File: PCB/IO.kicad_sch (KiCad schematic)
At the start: 18 parts, among them J6 USB_1, J7 USB_2, U11 FUSB_1, U13 FUSB_2, U5 TS3USB_2, U7 TS3USB_1

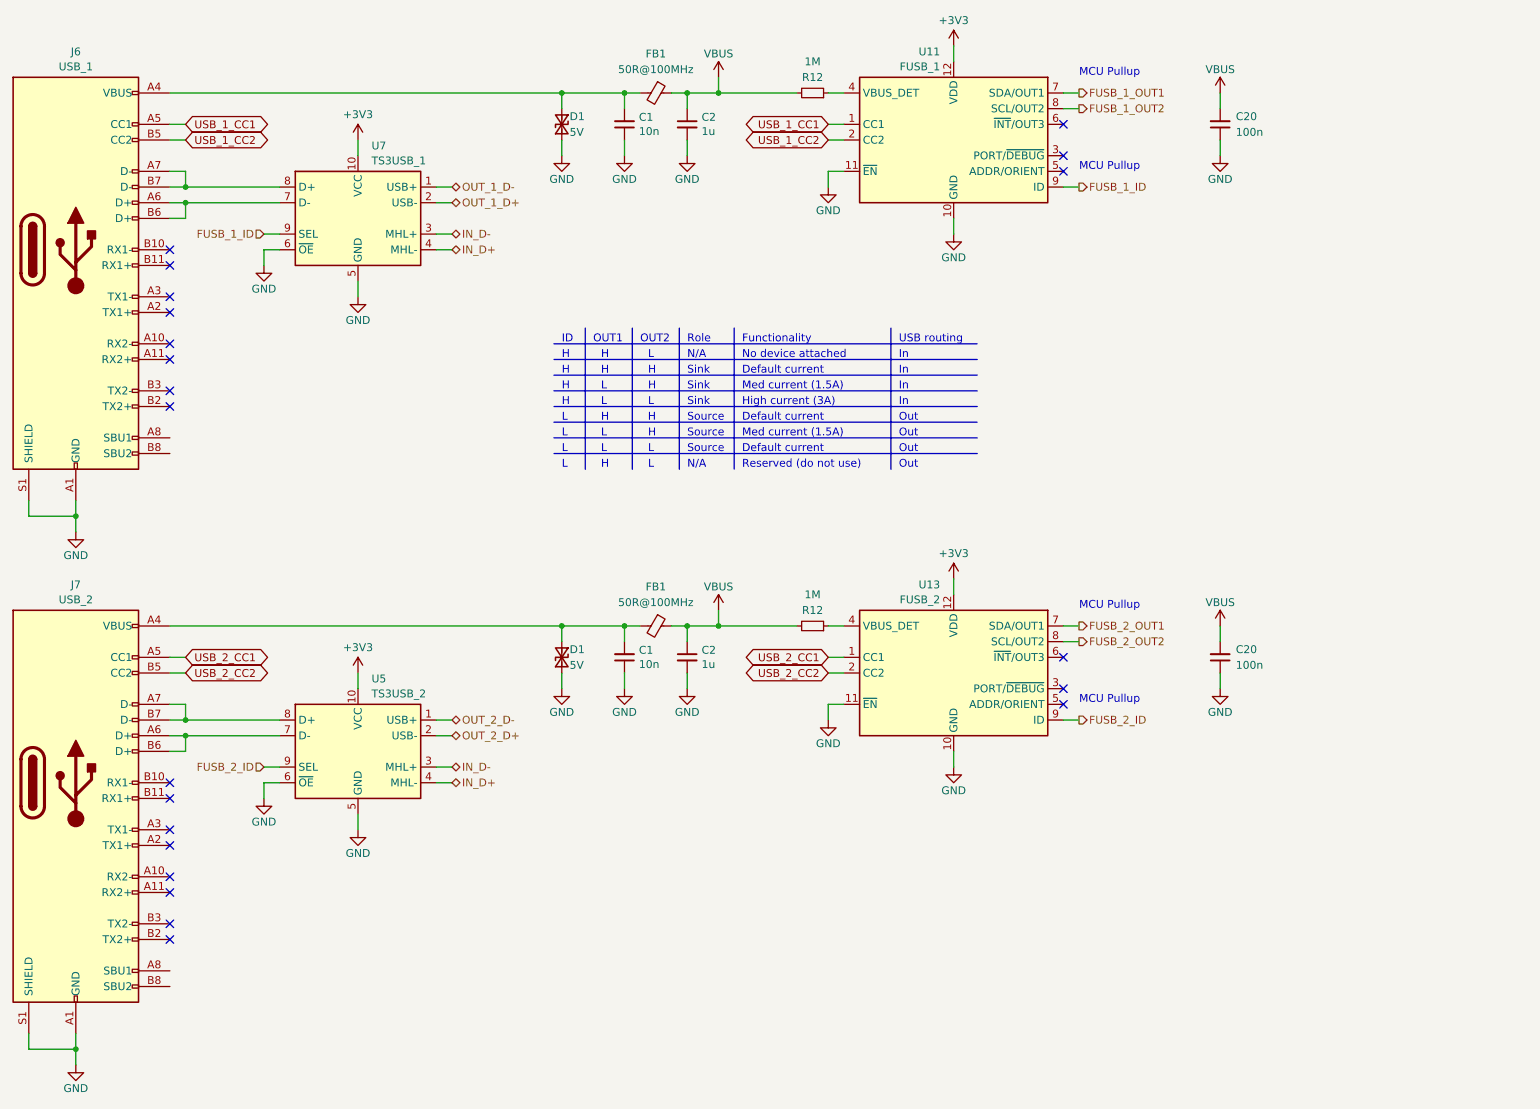
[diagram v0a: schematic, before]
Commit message: 23/08/2023 update
Changed MCU to nRF52840. Added nPM1300 PMIC for power management. Replaced SSD1351 display with Nice!View. Added Kailh Choc V1/V2 and Gateron KS-27/KS-33 support.
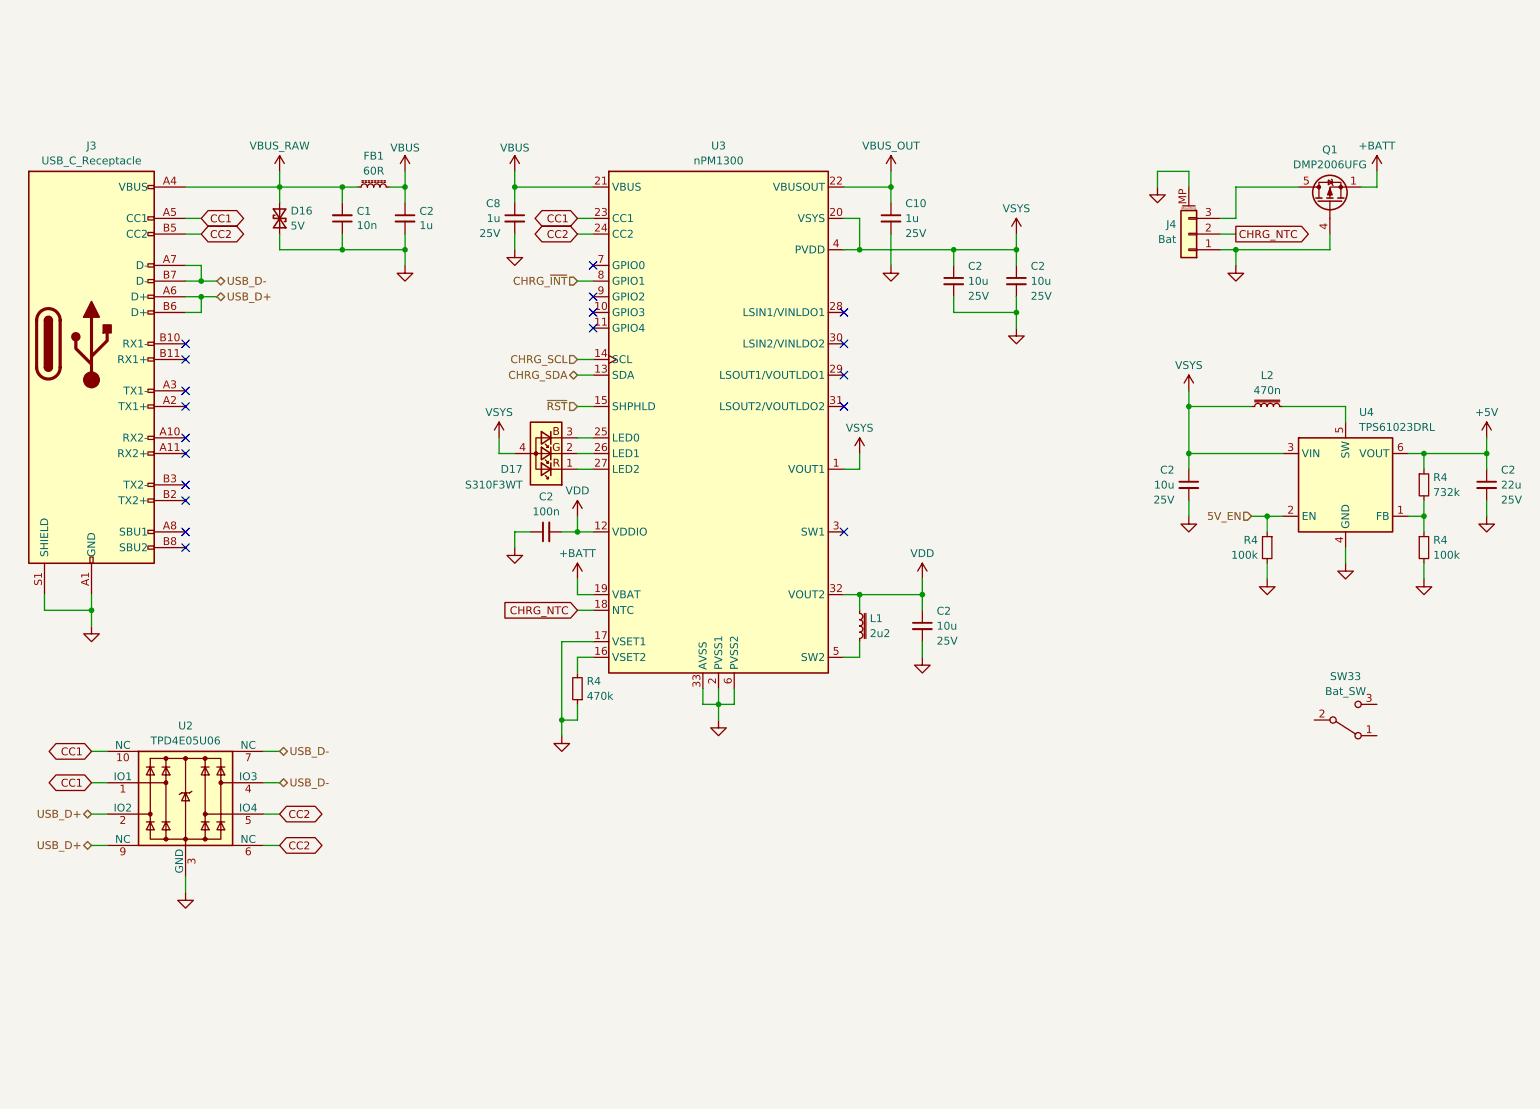
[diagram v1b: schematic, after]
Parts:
- removed C1 (x2): 10n, Capacitor_SMD:C_0402_1005Metric, symbol Device:C_Small
- removed C2 (x2): 1u, Capacitor_SMD:C_0603_1608Metric, symbol Device:C_Small
- removed C20 (x2): 100n, Capacitor_SMD:C_0402_1005Metric, symbol Device:C_Small
- removed D1 (x2): 5V, Diode_SMD:D_SOD-523, symbol Galia:D_TVS_Small
- removed FB1 (x2): 50R@100MHz, Inductor_SMD:L_1206_3216Metric, symbol Device:FerriteBead_Small
- removed J6: USB_1, symbol Connector:USB_C_Receptacle
- removed J7: USB_2, symbol Connector:USB_C_Receptacle
- removed R12 (x2): 1M, Resistor_SMD:R_0402_1005Metric, symbol Device:R_Small
- removed U11: FUSB_1, Package_DFN_QFN:Texas_X2QFN-12_1.6x1.6mm_P0.4mm, symbol Cantaloupe:FUSB303B
- removed U13: FUSB_2, Package_DFN_QFN:Texas_X2QFN-12_1.6x1.6mm_P0.4mm, symbol Cantaloupe:FUSB303B
- removed U5: TS3USB_2, symbol Cantaloupe:TS3USB3000
- removed U7: TS3USB_1, symbol Cantaloupe:TS3USB3000
- added C1: 10n, Ariamelon-Device:C_0402_1005Metric, symbol Device:C_Small
- added C10, C8: 1u, Ariamelon-Device:C_0402_1005Metric, symbol Device:C_Small
- added C2: 100n, Ariamelon-Device:C_0402_1005Metric, symbol Device:C_Small
- added C2 (x4): 10u, Ariamelon-Device:C_0603_1608Metric, symbol Device:C_Small
- added C2: 1u, Ariamelon-Device:C_0603_1608Metric, symbol Device:C_Small
- added C2: 22u, Ariamelon-Device:C_0805_2012Metric, symbol Device:C_Small
- added D16: 5V, Diode_SMD:D_SOD-523, symbol Ariamelon-Device:D_TVS_Small
- added D17: S310F3WT, Ariamelon-Device:LED_Lite-On_LTST-S310_3x1.5mm_Horizontal, symbol Ariamelon-Device:LED_ABGR_Small
- added FB1: 60R, Ariamelon-Device:L_0805_2012Metric, symbol Device:L_Ferrite_Small
- added J3: USB_C_Receptacle, Ariamelon-Connector:Hirose_CX70M-24P1, symbol Connector:USB_C_Receptacle
- added J4: Bat, Ariamelon-Connector:JST_SH_SM03B-SRSS-TB_1x03-1MP_P1.00mm_Horizontal, symbol Connector_Generic_MountingPin:Conn_01x03_MountingPin
- added L1: 2u2, Ariamelon-Device:L_Murata_DFE201610P, symbol Device:L_Iron_Small
- added L2: 470n, Ariamelon-Device:L_Murata_DFE201610P, symbol Device:L_Iron_Small
- added Q1: DMP2006UFG, Ariamelon-Package:Diodes_PowerDI3333-8, symbol Transistor_FET:DMP3013SFV
- added R4: 732k, Ariamelon-Device:R_0402_1005Metric, symbol Device:R_Small
- added R4: 470k, Ariamelon-Device:R_0402_1005Metric, symbol Device:R_Small
- added R4 (x2): 100k, Ariamelon-Device:R_0402_1005Metric, symbol Device:R_Small
- added SW33: Bat_SW, Button_Switch_SMD:SW_SPDT_PCM12, symbol Switch:SW_SPDT
- added U2: TPD4E05U06, Ariamelon-Package:USON-10_2.5x1.0mm_P0.5mm, symbol Ariamelon-IC:TPD4E05U06
- added U3: nPM1300, Ariamelon-Package:QFN-32-1EP_5x5mm_P0.5mm_EP3.5x3.5mm, symbol Ariamelon-IC:nPM1300
- added U4: TPS61023DRL, Ariamelon-Package:SOT-563, symbol Ariamelon-IC:TPS61023DRL
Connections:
- net GND: now also C1.1, C10.2, C2.1, C2.2, C2.2, C2.2, C2.2, C2.2, C2.2, C8.2, D16.1 (K), J3.A1 (GND), J3.A12 (GND), J3.B1 (GND), J3.B12 (GND), J3.S1 (SHIELD), J4.1 (Pin_1), J4.MP (MountPin), Q1.4 (G), R4.1, R4.2, R4.2, U2.3 (GND), U2.8 (GND), U3.17 (VSET1), U3.2 (PVSS1), U3.33 (AVSS), U3.6 (PVSS2), U4.4 (GND)
- net VBUS: now also C2.1, C8.1, FB1.1, U3.21 (VBUS)
- new net: D17.1 (RK), U3.27 (LED2)
- new net: D17.2 (GK), U3.26 (LED1)
- new net: D17.3 (BK), U3.25 (LED0)
- new net: R4.1, R4.2, U4.1 (FB)
- new net: L2.2, U4.5 (SW)
- new net: J4.3 (Pin_3), Q1.5 (D)
- new net: R4.2, U3.16 (VSET2)
- new net: L1.2, U3.5 (SW2)
- new net +5V: C2.1, R4.1, U4.6 (VOUT)
- new net +BATT: Q1.1 (S), Q1.2 (S), Q1.3 (S), U3.19 (VBAT)
- new net 5V_EN: R4.1, U4.2 (EN)
- new net CC1: J3.A5 (CC1), U2.1 (IO1), U2.10 (NC), U3.23 (CC1)
- new net CC2: J3.B5 (CC2), U2.5 (IO4), U2.6 (NC), U3.24 (CC2)
- new net CHRG_NTC: J4.2 (Pin_2), U3.18 (NTC)
- new net CHRG_SCL: U3.14 (SCL)
- new net CHRG_SDA: U3.13 (SDA)
- new net CHRG_~{INT}: U3.8 (GPIO1)
- new net USB_D+: J3.A6 (D+), J3.B6 (D+), U2.2 (IO2), U2.9 (NC)
- new net USB_D-: J3.A7 (D-), J3.B7 (D-), U2.4 (IO3), U2.7 (NC)
- new net VBUS_OUT: C10.1, U3.22 (VBUSOUT)
- new net VBUS_RAW: C1.2, D16.2 (A), FB1.2, J3.A4 (VBUS), J3.A9 (VBUS), J3.B4 (VBUS), J3.B9 (VBUS)
- new net VDD: C2.1, C2.2, L1.1, U3.12 (VDDIO), U3.32 (VOUT2)
- new net VSYS: C2.1, C2.1, C2.1, D17.4 (A), L2.1, U3.1 (VOUT1), U3.20 (VSYS), U3.4 (PVDD), U4.3 (VIN)
- new net ~{RST}: U3.15 (SHPHLD)
- no-connect marks 22 -> 19
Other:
- note removed: "Default current"
- note removed: "Functionality"
- note removed: "H"
- note removed: "High current (3A)"
- note removed: "ID"
- note removed: "In"
- note removed: "L"
- note removed: "MCU Pullup"
- note removed: "Med current (1.5A)"
- note removed: "N/A"
- note removed: "No device attached"
- note removed: "OUT1"
- note removed: "OUT2"
- note removed: "Out"
- note removed: "Reserved (do not use)"
- note removed: "Role"
- note removed: "Sink"
- note removed: "Source"
- note removed: "USB routing"
- company: Created by Ariamelon (https://github.com/Ariamelon/Cantaloupe/) -> (none)
- title: Cantaloupe split ergonomic keyboard -> (none)

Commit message: 24/08/2023 update
Finished routing. Consolidated all libraries into Ariamelon's Kicad Master Library. Added PCM12 switch connected to nPM1300 GPIO. Rearranged components and rerouted.
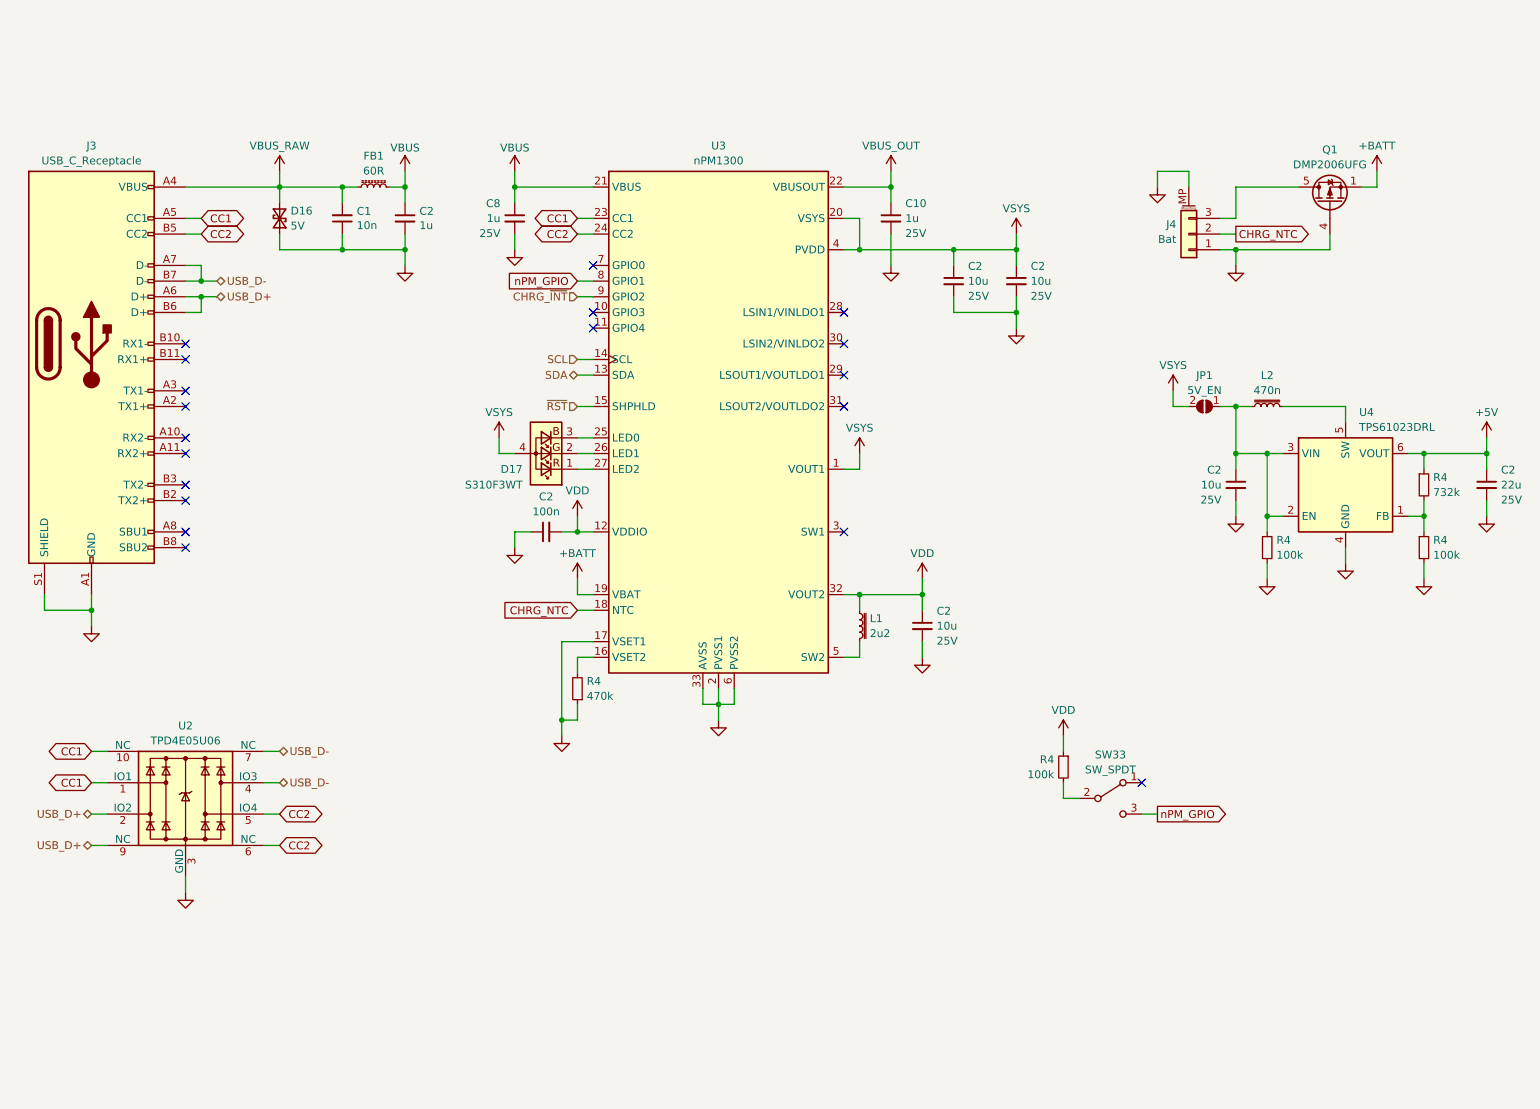
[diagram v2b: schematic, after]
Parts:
- added JP1: 5V_EN, Jumper:SolderJumper-2_P1.3mm_Open_Pad1.0x1.5mm, symbol Cantaloupe:SolderJumper_2_Open
- added R4: 100k, Ariamelon-Device:R_0402_1005Metric, symbol Device:R_Small
- SW33: value Bat_SW -> SW_SPDT; footprint Button_Switch_SMD:SW_SPDT_PCM12 -> Ariamelon-Switch:SW_CK_SPDT_PCM12; LCSC C963206 -> (none)
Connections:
- net CHRG_~{INT}: now also U3.9 (GPIO2); no longer U3.8 (GPIO1)
- net VDD: now also R4.1
- net VSYS: now also JP1.2 (B); no longer C2.1, L2.1, U4.3 (VIN)
- net at SW33.2 (B): now also R4.2
- net nPM_GPIO: now reaches SW33.3 (C)
- net nPM_GPIO: now also U3.8 (GPIO1)
- net 5V_EN: no longer names the net of R4.1, U4.2 (EN)
- net 5V_EN: now also C2.1, L2.1, U4.3 (VIN), JP1.1 (A)
- net CHRG_SCL renamed SCL
- net CHRG_SDA renamed SDA
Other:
- moved on the sheet: C2
